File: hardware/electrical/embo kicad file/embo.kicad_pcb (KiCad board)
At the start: 2 copper layers, 96.4 x 48.3 mm, 101 parts, among them IC1 OPA2354, IC2 OPA2354, J1 Conn_Coaxial, J10 Conn_01x08, J11 Conn_01x08, J12 Conn_01x08, J13 USB_C_Receptacle_USB2.0_16P, J14 24 V PSU input, J15 Conn_01x08, J2 Conn_Coaxial, J3 UART to RPi, J4 JSTXH 6pin Socket 1, J5 JSTXH 6pin Socket 2, J6 motor 1, J7 motor 2, J8 LED Panel, J9 Conn_02x10_Odd_Even, Q1 AO4407A, U1 ESP32-S3-WROOM-1, U2 LM2596S-5, U3 AMS1117-3.3, U4 AD9833xRM

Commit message: Finish main PCB layout, starting routing
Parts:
- removed C29, C40: 100nF X7R, Capacitor_SMD:C_0402_1005Metric_Pad0.74x0.62mm_HandSolder
- removed C32: 10µF X5R 0805, Capacitor_SMD:C_0805_2012Metric
- moved D1 50.9 mm to (173.7, 109.7)
- moved C26 47.6 mm to (181.1, 102.9), turned to 180 degrees
- moved D2 47.2 mm to (188.1, 108.0), turned to 180 degrees
- moved D3 44.9 mm to (190.8, 104.6), turned to 180 degrees
- moved C21 44.3 mm to (176.8, 104.0), turned to 180 degrees
- moved C_env1 42.9 mm to (187.8, 105.2), turned to 180 degrees
- moved C20 41.5 mm to (176.2, 108.0), turned to 90 degrees
- moved R28 41.2 mm to (174.3, 106.4)
- moved C25 38.8 mm to (183.4, 102.9), turned to 90 degrees
- moved C_adc1 38.2 mm to (191.5, 102.1)
- moved R26 37.1 mm to (176.8, 106.0)
- moved R35 37.0 mm to (176.8, 105.0), turned to 180 degrees
- moved IC2 36.7 mm to (181.9, 106.7)
- moved R_in1 35.4 mm to (176.2, 110.3), turned to 90 degrees
- moved R_env1 34.3 mm to (187.6, 106.2), turned to 180 degrees
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
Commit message: PCB trace routing update 50%
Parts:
- moved D5 16.2 mm to (117.1, 73.7), turned to 0 degrees
- moved Cbuck1 11.3 mm to (120.1, 87.1), turned to -90 degrees
- moved C12 4.41 mm to (163.8, 76.0), turned to -90 degrees
- moved C11 1.63 mm to (165.6, 74.6), turned to -90 degrees
- moved R41 1.61 mm to (171.7, 106.2), turned to 0 degrees
- moved J6 1.52 mm to (160.6, 85.9)
- moved J3 1.52 mm to (164.3, 91.9)
- moved J7 1.52 mm to (168.4, 85.9)
- moved F1 1.47 mm to (109.2, 74.4)
- moved C41 1.42 mm to (168.9, 106.2)
- moved C17 1.29 mm to (163.3, 79.2)
- moved C18 1.29 mm to (166.7, 79.2)
- moved C23 1.23 mm to (158.6, 97.8)
- moved C24 1.23 mm to (161.0, 97.8)
- moved C30 1.05 mm to (171.2, 98.0)
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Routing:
- net +24V: track 0.00 -> 88.9 mm
- net GND: track 0.00 -> 43.1 mm, vias 0 -> 15
- net +3V3: track 0.00 -> 32.4 mm, vias 0 -> 12
- net Net-(D4-K): track 0.00 -> 16.9 mm
- net Net-(U1-IO0): track 0.00 -> 16.4 mm
- net Net-(IC2-+INB): track 0.00 -> 15.2 mm
- net /UAS_ADC: track 0.00 -> 12.3 mm
- net Net-(IC1-+INA): track 0.00 -> 11.4 mm
- net /TX_OUT: track 0.00 -> 8.35 mm
- net /M1_B2: track 0.00 -> 7.67 mm
- net /M2_B2: track 0.00 -> 7.65 mm
- net Net-(IC2--INB): track 0.00 -> 7.41 mm
- net /M1_A1: track 0.00 -> 6.67 mm
- net /M2_A1: track 0.00 -> 6.65 mm
- net /M1_B1: track 0.00 -> 6.65 mm
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- added copper zone on F.Cu, net +24V
- added copper zone on F.Cu, net +3V3
- added copper zone on In2.Cu, net +3V3
- added copper zone on F.Cu, net +5V
- added copper zone on In1.Cu, net GND
- added copper zone on F.Cu, net Net-(D7-K)
- added copper zone on F.Cu, net Net-(F1-Pad1)
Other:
- copper layers 2 -> 4

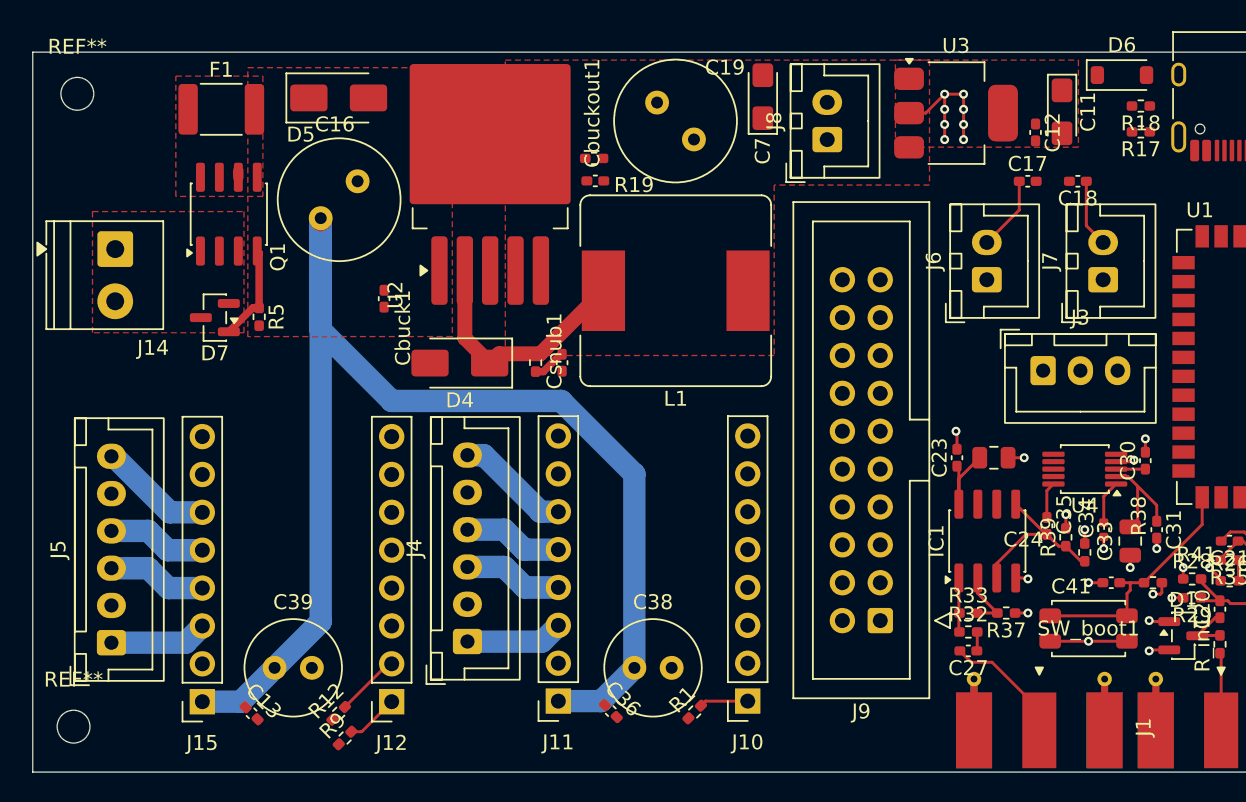
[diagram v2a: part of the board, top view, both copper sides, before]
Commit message: fix LM2596S-5 Buck Converter Footprint pinout mismatch and reroute buck converter block to minimise switching circuit loop area
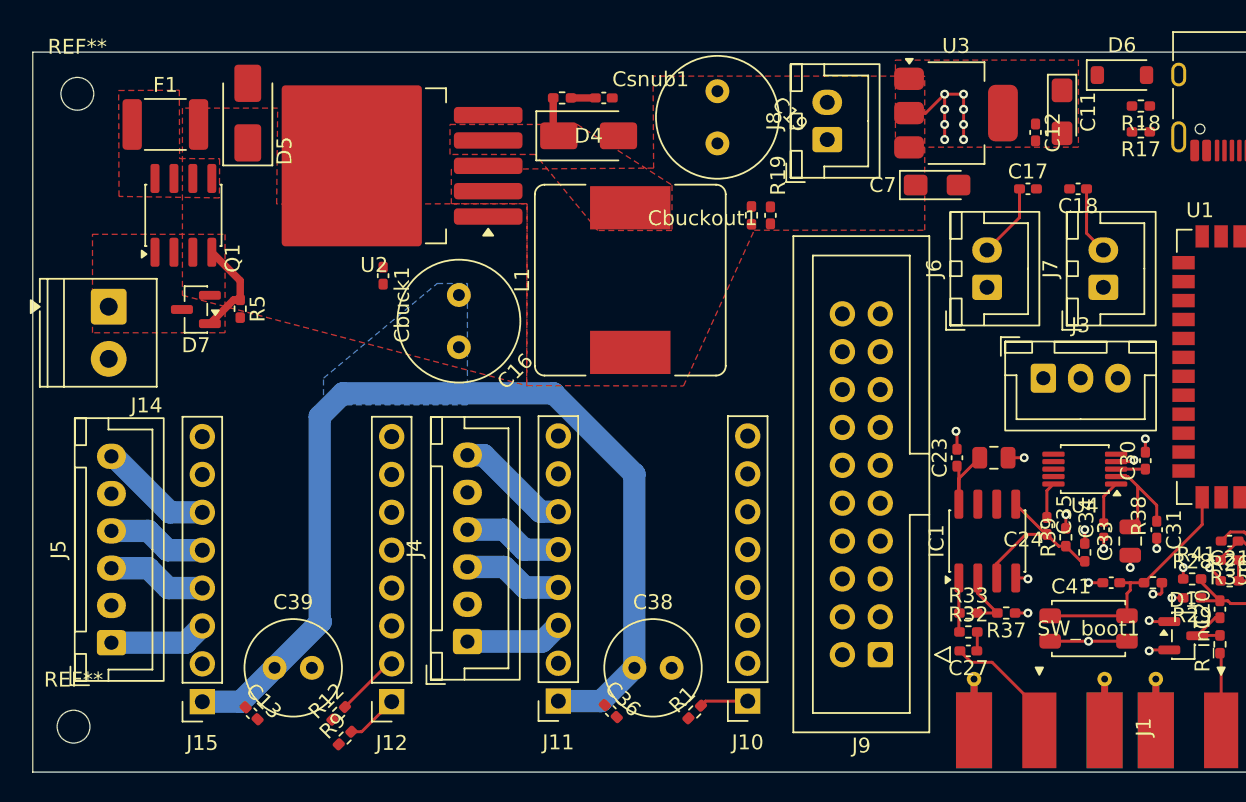
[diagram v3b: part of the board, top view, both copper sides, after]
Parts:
- moved Csnub1 18.0 mm to (134.9, 73.7), turned to 0 degrees
- moved Rsnub1 17.8 mm to (132.1, 73.7), turned to 0 degrees
- moved D4 17.5 mm to (133.9, 76.2), turned to 0 degrees
- moved C7 13.1 mm to (157.2, 79.5), turned to 0 degrees
- moved Cbuckout1 12.0 mm to (146.1, 81.5), turned to -90 degrees
- moved R19 11.2 mm to (144.8, 81.5), turned to -90 degrees
- moved C16 10.6 mm to (125.2, 86.9), turned to -90 degrees
- moved U2 7.81 mm to (119.5, 78.2), turned to 180 degrees
- moved D5 6.18 mm to (111.0, 74.7), turned to 90 degrees
- moved J14 3.89 mm to (101.7, 87.7)
- moved F1 3.88 mm to (105.5, 75.4)
- moved L1 3.13 mm to (136.7, 85.9), turned to 90 degrees
- moved Q1 3.05 mm to (106.7, 81.5)
- moved J9 2.29 mm to (153.4, 111.0)
- moved C19 1.59 mm to (142.5, 76.7), turned to 90 degrees
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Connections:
- U2 pad 2: Net-(D4-K) -> +5V
- U2 pad 4: +5V -> Net-(D4-K)
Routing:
- net +24V: track 88.9 -> 67.0 mm
- net Net-(D4-K): track 16.9 -> 2.70 mm
- net Net-(Csnub1-Pad1): track 2.26 -> 1.63 mm
- added copper zone on B.Cu, net +24V
- added copper zone on F.Cu, net Net-(D4-K)

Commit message: signal routing update  70%
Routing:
- net /EC11_A (CLK): track 0.00 -> 48.4 mm
- net /EC11_B (DT): track 0.00 -> 44.3 mm
- net /TFT_CS: track 0.00 -> 40.4 mm
- net /EC11_SW: track 0.00 -> 39.2 mm
- net /TFT_RST: track 0.00 -> 37.8 mm
- net /TOUCH_CS: track 0.00 -> 35.8 mm
- net +5V: track 0.00 -> 35.3 mm
- net /TFT_DC: track 0.00 -> 33.6 mm
- net /SPI_MISO: track 0.00 -> 30.9 mm
- net /SPI_CLK: track 0.00 -> 28.6 mm
- net /BUZ_PWM: track 0.00 -> 28.1 mm
- net /SPI_MOSI: track 0.00 -> 28.0 mm
- net GND: track 43.1 -> 70.4 mm
- net /TOUCH_IRQ: track 0.00 -> 23.4 mm
- net /BTN1: track 0.00 -> 23.3 mm
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
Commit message: main PCB routing update 90%
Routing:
- net Net-(J10-Pin_4): track 1.52 -> 126.3 mm, vias 0 -> 1
- net GND: track 70.4 -> 112.8 mm, vias 15 -> 123
- net Net-(J13-CC1): track 0.00 -> 28.1 mm
- net +5V: track 35.3 -> 54.4 mm
- net +24V: track 67.0 -> 85.6 mm, vias 0 -> 24
- net /AD9833_SC: track 0.00 -> 17.8 mm, vias 0 -> 2
- net /M2_DIR: track 0.00 -> 17.1 mm
- net /M2_STEP: track 0.00 -> 13.6 mm
- net Net-(J13-CC2): track 0.00 -> 8.08 mm
- net /SPI_CLK: track 28.6 -> 32.8 mm, vias 0 -> 2
- net /SPI_MOSI: track 28.0 -> 31.1 mm, vias 0 -> 2
- net +3V3: track 41.5 -> 44.6 mm, vias 12 -> 25
- net /BTN2: track 22.2 -> 24.3 mm, vias 0 -> 1
- net /TFT_CS: track 40.4 -> 42.4 mm, vias 0 -> 1
- net /EC11_B (DT): track 44.3 -> 46.2 mm, vias 0 -> 1
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- added copper zone on F.Cu, net GND

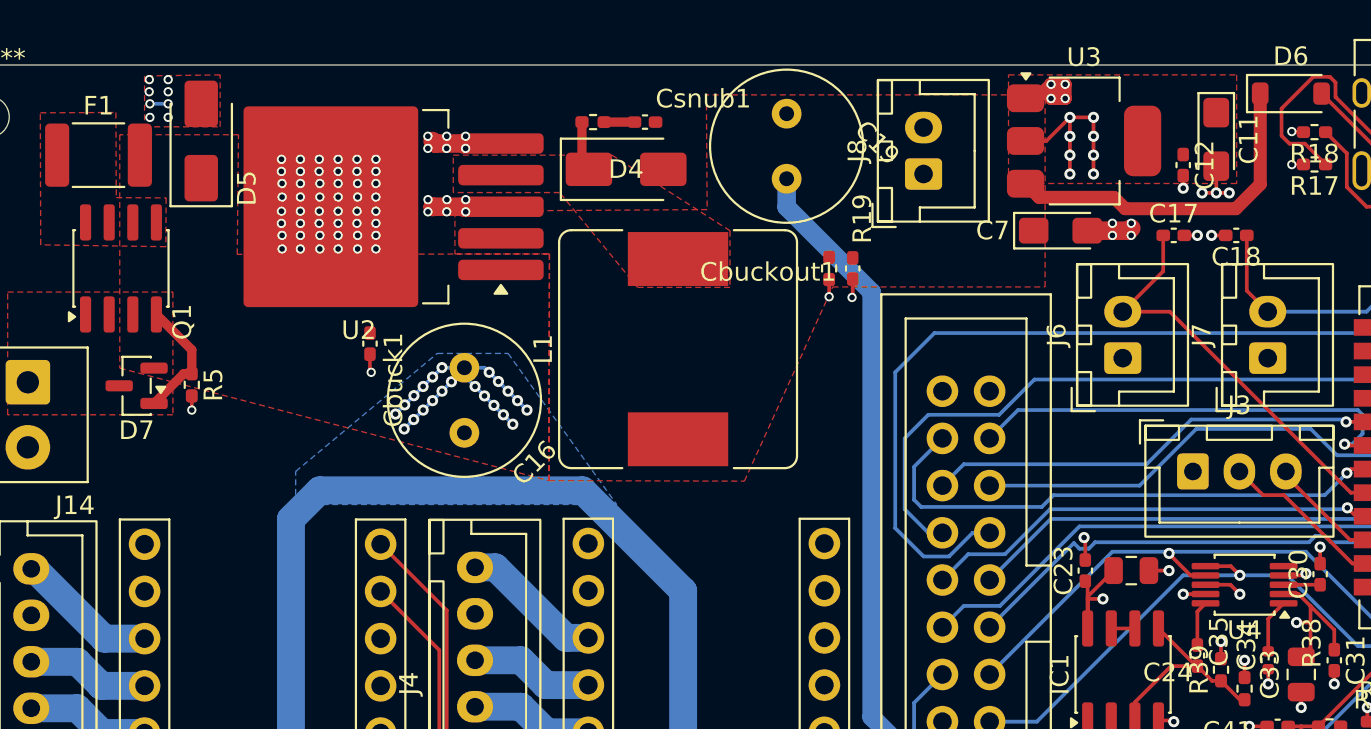
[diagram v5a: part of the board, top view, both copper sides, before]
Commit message: PCB main added EMI shield (heavily stitched GND plane) between buck - UAS block
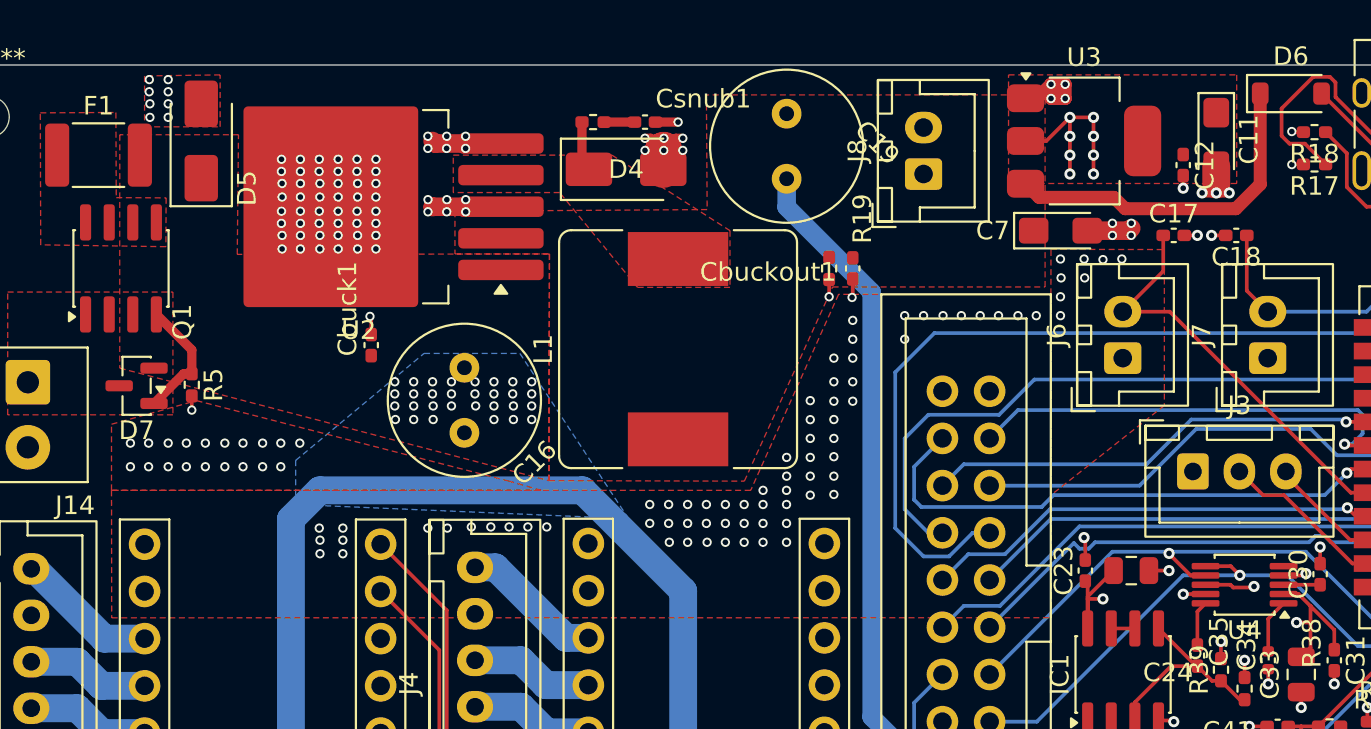
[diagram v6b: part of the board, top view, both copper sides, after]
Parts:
- moved Cbuck1 0.10 mm to (120.1, 85.7), turned to 90 degrees
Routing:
- net +24V: track 85.6 -> 67.8 mm, vias 24 -> 32
- net GND: track 112.8 -> 116.3 mm, vias 123 -> 225

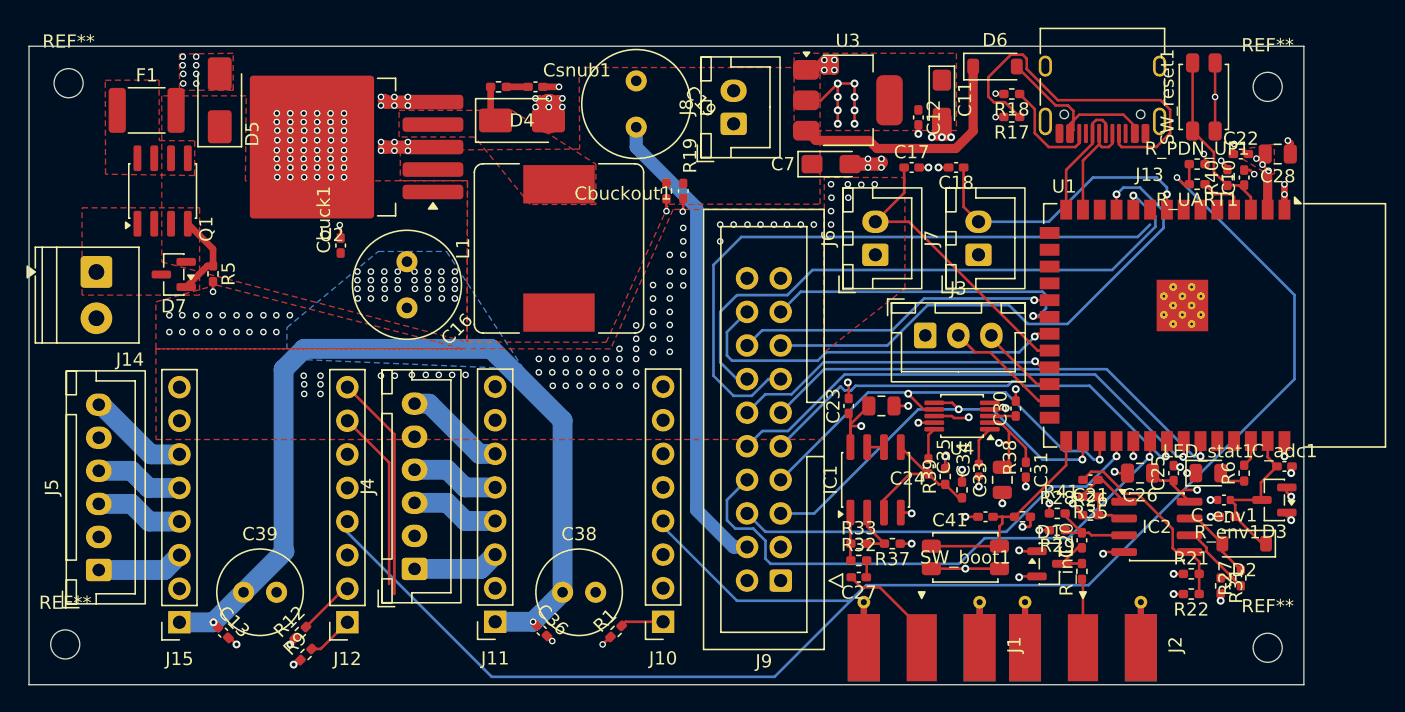
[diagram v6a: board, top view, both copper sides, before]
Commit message: fixed silkscreen on main PCB
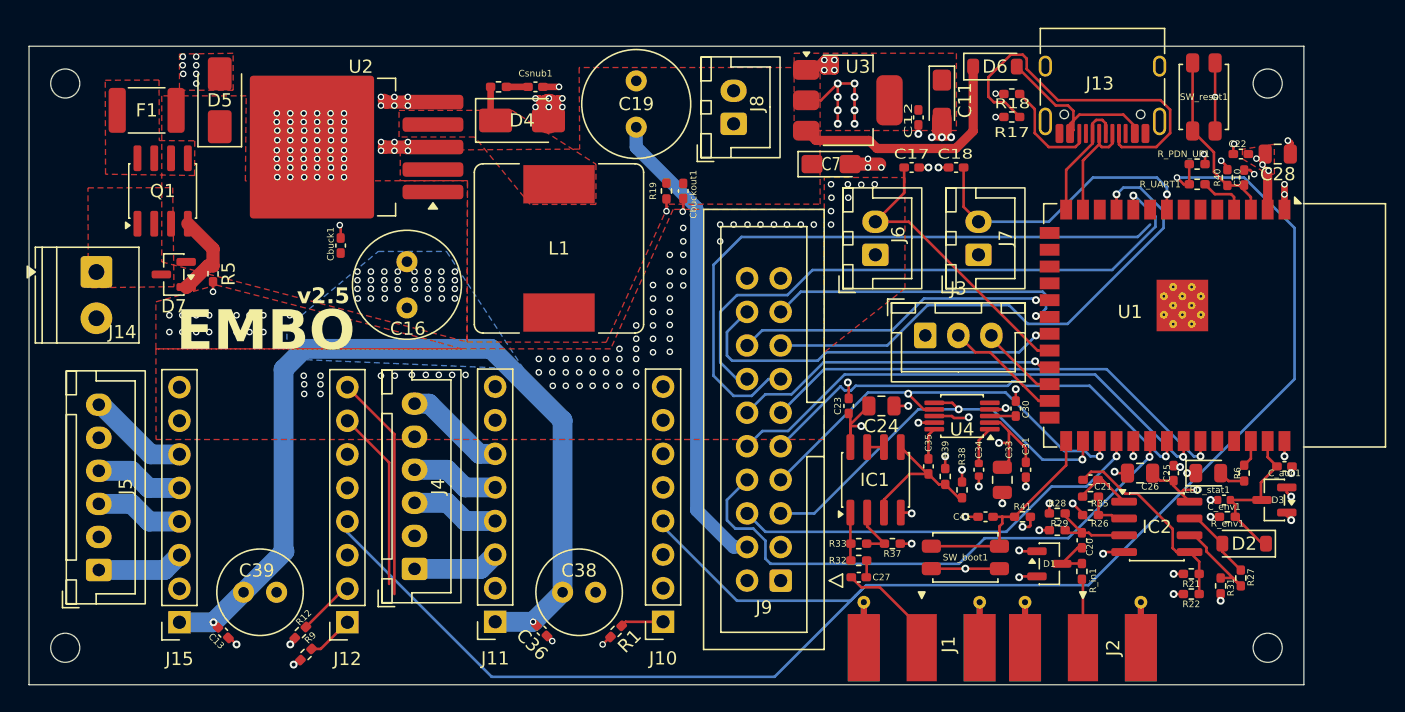
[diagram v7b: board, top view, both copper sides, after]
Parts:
- moved REF** 0.26 mm to (99.3, 73.4)
- moved REF** 0.25 mm to (99.3, 116.1)
- moved REF** 0.25 mm to (190.2, 73.4)
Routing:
- net Net-(J10-Pin_4): track 126.3 -> 129.3 mm
- net GND: track 116.3 -> 116.1 mm, vias 225 -> 223
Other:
- board text added: "EMBO"
- board text added: "v2.5"
